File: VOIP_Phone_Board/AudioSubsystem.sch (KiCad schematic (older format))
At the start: 39 parts, among them J1 Headset, J5 Speaker, J6 Microphone, U1 PCM5102, U2 PCM1808PW, X1 SG-8002DC

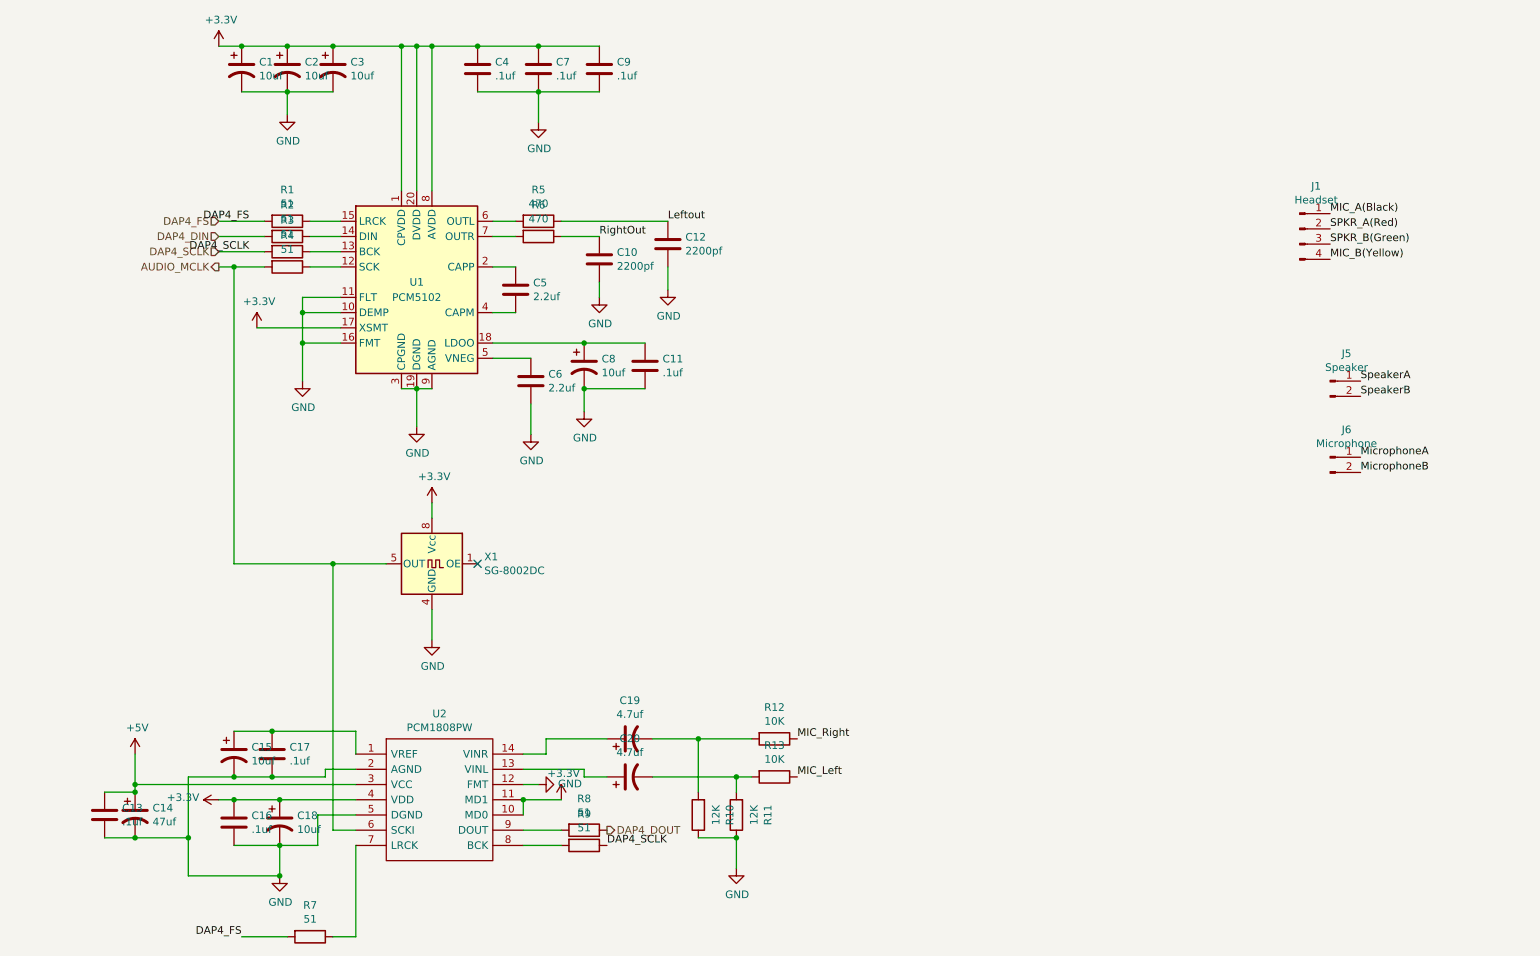
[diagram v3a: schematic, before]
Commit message: MAX98357A Version.
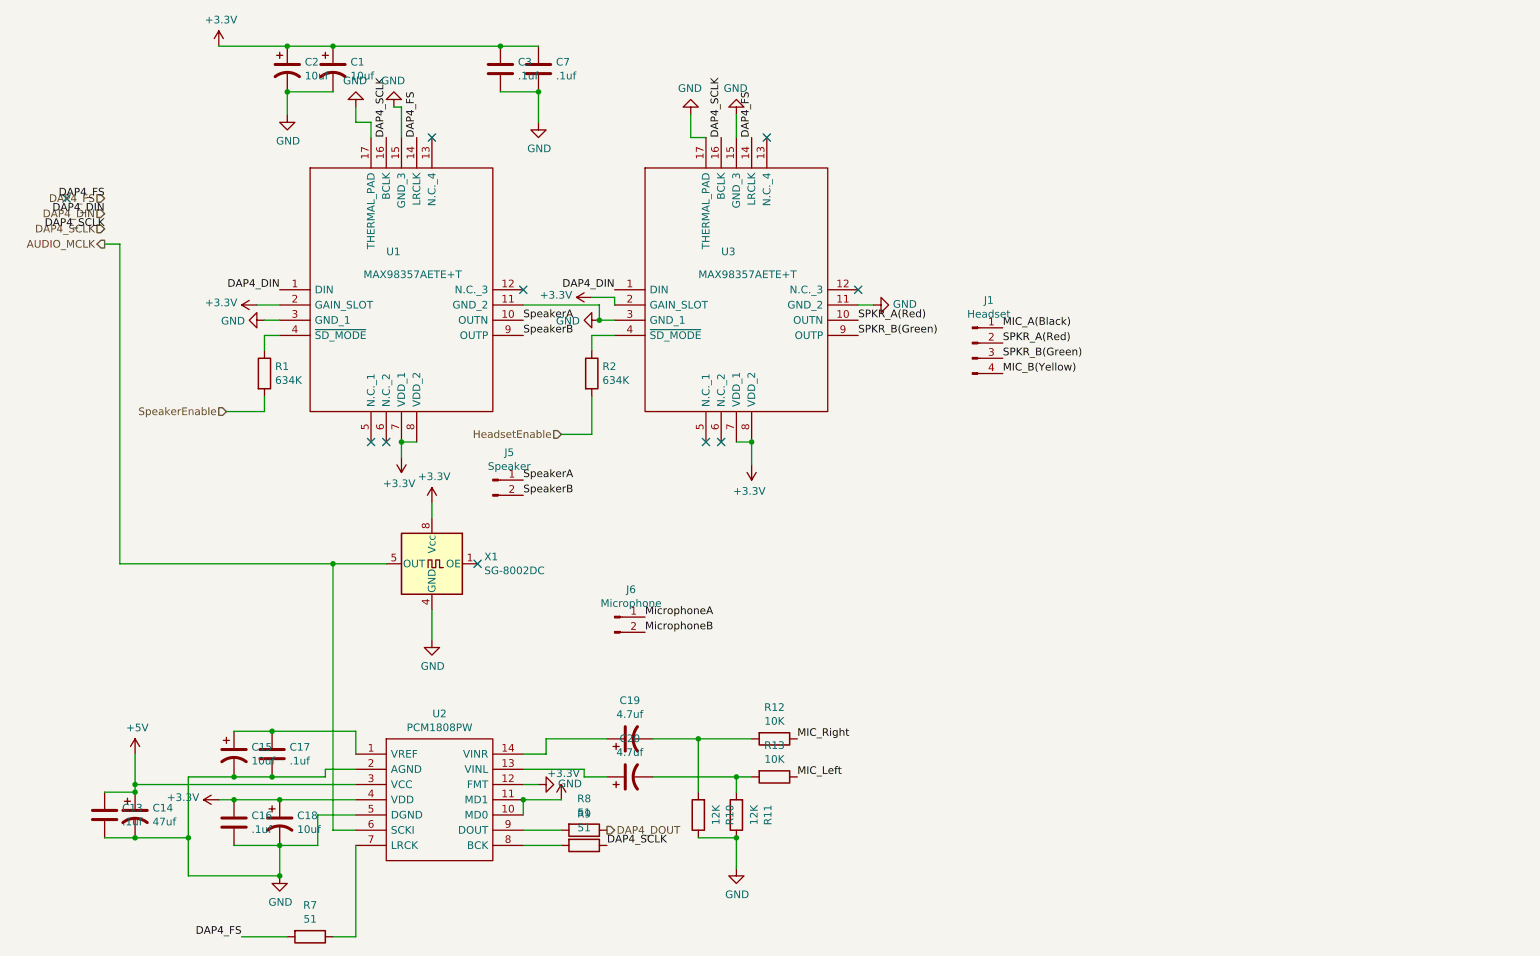
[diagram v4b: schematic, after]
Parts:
- removed C10, C12: 2200pf, Capacitor_THT:C_Rect_L4.0mm_W2.5mm_P2.50mm, symbol Device:C
- removed C11, C4, C9: .1uf, Capacitor_SMD:C_0603_1608Metric_Pad1.05x0.95mm_HandSolder, symbol Device:C
- removed C3, C8: 10uf, VOIP_Phone_Board:CP_0603_1608Metric_Pad1.05x0.95mm_HandSolder, symbol Device:CP1
- removed C5, C6: 2.2uf, Capacitor_SMD:C_0402_1005Metric, symbol Device:C
- removed R3, R4: 51, Resistor_SMD:R_0603_1608Metric_Pad1.05x0.95mm_HandSolder, symbol Device:R
- removed R5, R6: 470, Resistor_SMD:R_0603_1608Metric_Pad1.05x0.95mm_HandSolder, symbol Device:R
- removed U1: PCM5102, Package_SO:TSSOP-20_4.4x6.5mm_P0.65mm, symbol Audio:PCM5102
- added C3: .1uf, Capacitor_SMD:C_0603_1608Metric_Pad1.05x0.95mm_HandSolder, symbol Device:C
- added U1, U3: MAX98357AETE+T, QFN50P300X300X80-17N, symbol MAX98357AETE+T:MAX98357AETE+T
- R1, R2: value 51 -> 634K; Mouser Part Number 667-ERJ-PA3J510V -> 603-RT0603FRE07634KL
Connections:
- net +3V3: now also C3.1, U1.2 (GAIN_SLOT), U1.7 (VDD_1), U1.8 (VDD_2), U3.2 (GAIN_SLOT), U3.7 (VDD_1), U3.8 (VDD_2)
- net DAP4_DIN: now also U1.1 (DIN), U3.1 (DIN); no longer R2.2
- net DAP4_FS: now also U1.14 (LRCLK), U3.14 (LRCLK); no longer R1.2
- net DAP4_SCLK: now also U1.16 (BCLK), U3.16 (BCLK)
- net GND: now also C3.2, U1.11 (GND_2), U1.15 (GND_3), U1.17 (THERMAL_PAD), U1.3 (GND_1), U3.11 (GND_2), U3.15 (GND_3), U3.17 (THERMAL_PAD), U3.3 (GND_1)
- net SPKR_A(Red): now also U3.10 (OUTN)
- net SPKR_B(Green): now also U3.9 (OUTP)
- net SpeakerA: now also U1.10 (OUTN)
- net SpeakerB: now also U1.9 (OUTP)
- net at R2.1: now also U3.4 (~SD_MODE)
- net at R1.1: now also U1.4 (~SD_MODE)
- new net HeadsetEnable: R2.2
- new net SpeakerEnable: R1.2
- no-connect marks 1 -> 10
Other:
- moved on the sheet: J1, J5, J6

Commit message: Started with ADAU1361.
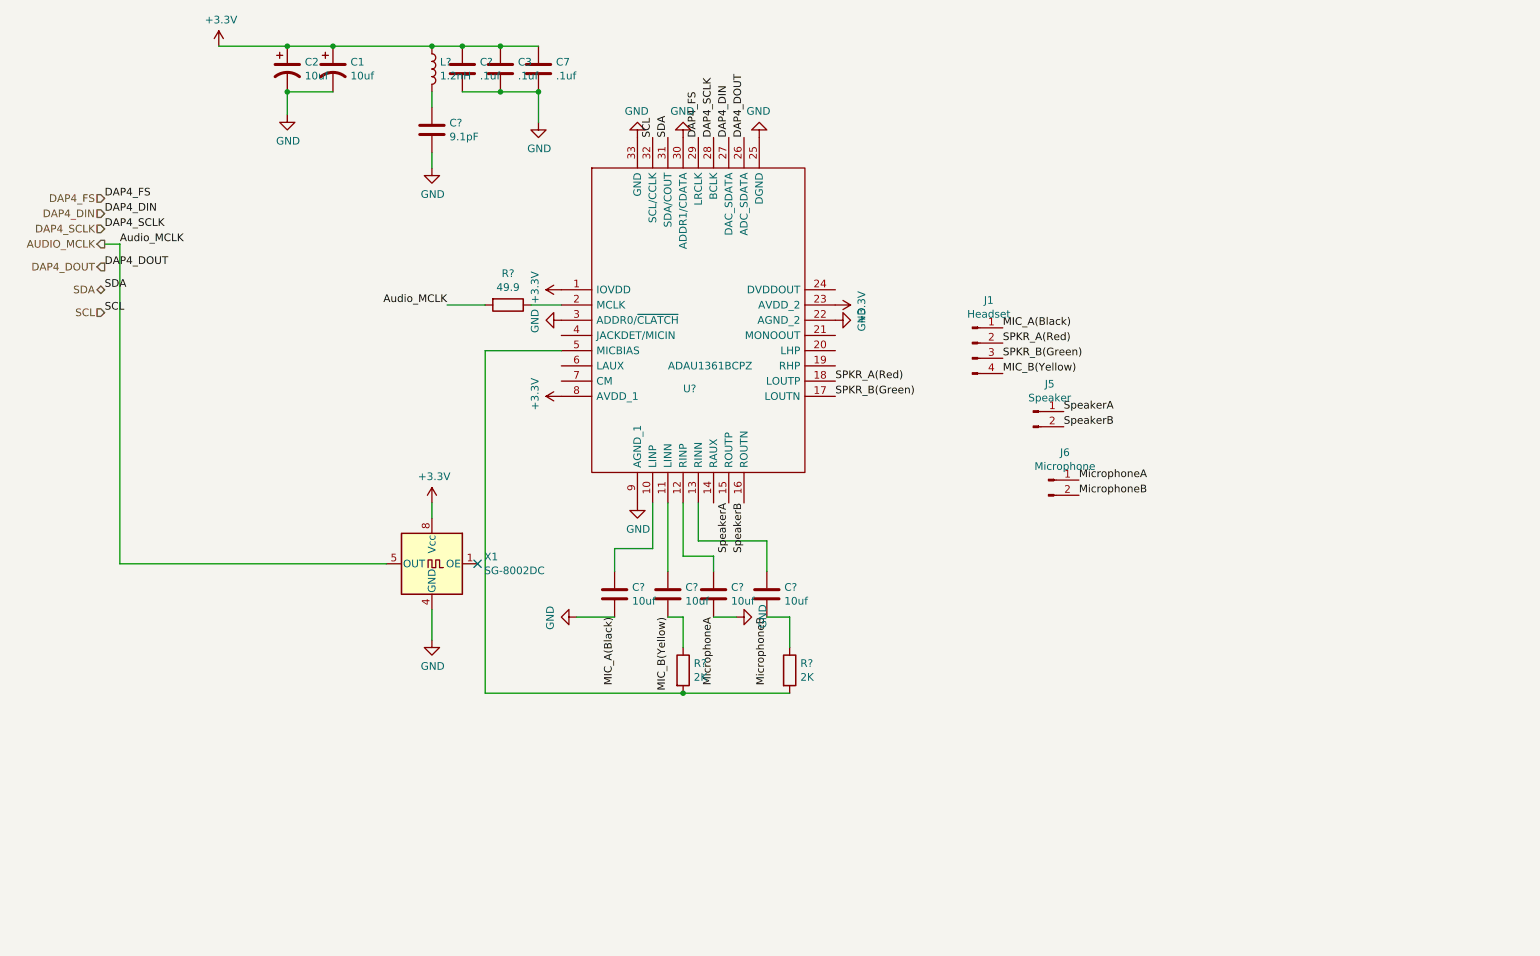
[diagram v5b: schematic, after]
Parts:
- removed C13, C16, C17: .1uf, Capacitor_SMD:C_0603_1608Metric_Pad1.05x0.95mm_HandSolder, symbol Device:C
- removed C14: 47uf, Capacitor_THT:CP_Radial_D6.3mm_P2.50mm, symbol Device:CP1
- removed C15, C18: 10uf, VOIP_Phone_Board:CP_0603_1608Metric_Pad1.05x0.95mm_HandSolder, symbol Device:CP1
- removed C19, C20: 4.7uf, VOIP_Phone_Board:CP_0603_1608Metric_Pad1.05x0.95mm_HandSolder, symbol Device:CP1
- removed R1, R2: 634K, Resistor_SMD:R_0603_1608Metric_Pad1.05x0.95mm_HandSolder, symbol Device:R
- removed R10, R11: 12K, Resistor_SMD:R_0603_1608Metric_Pad1.05x0.95mm_HandSolder, symbol Device:R
- removed R12, R13: 10K, Resistor_SMD:R_0603_1608Metric_Pad1.05x0.95mm_HandSolder, symbol Device:R
- removed R7, R8, R9: 51, Resistor_SMD:R_0603_1608Metric_Pad1.05x0.95mm_HandSolder, symbol Device:R
- removed U1, U3: MAX98357AETE+T, QFN50P300X300X80-17N, symbol MAX98357AETE+T:MAX98357AETE+T
- removed U2: PCM1808PW, VOIP_Phone_Board:SOP65P640X120-14N, symbol PCM1808PW:PCM1808PW
- added C?: .1uf, Capacitor_SMD:C_0603_1608Metric_Pad1.05x0.95mm_HandSolder, symbol Device:C
- added C?: 9.1pF, symbol Device:C
- added C? (x4): 10uf, symbol Device:C
- added L?: 1.2nH, symbol Device:L
- added R? (x2): 2K, symbol Device:R
- added R?: 49.9, symbol Device:R
- added U?: ADAU1361BCPZ, QFN50P500X500X100-33N-D, symbol ADAU1361BCPZ:ADAU1361BCPZ
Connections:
- net MIC_A(Black) is gone; now on net GND: J1.1 (Pin_1)
- net MicrophoneA is gone; now on net GND: J6.1 (Pin_1)
- net +3V3: now also C?.1, L?.1, U?.1 (IOVDD), U?.23 (AVDD_2), U?.8 (AVDD_1)
- net AUDIO_MCLK: now also R?.2
- net DAP4_DIN: now also U?.27 (DAC_SDATA)
- net DAP4_DOUT: now also U?.26 (ADC_SDATA)
- net DAP4_FS: now also U?.29 (LRCLK)
- net DAP4_SCLK: now also U?.28 (BCLK)
- net GND: now also C?.2, C?.2, C?.2, C?.2, U?.22 (AGND_2), U?.25 (DGND), U?.3 (ADDR0/~CLATCH), U?.30 (ADDR1/CDATA), U?.33 (GND), U?.9 (AGND_1)
- net MIC_B(Yellow): now also C?.2, R?.1
- net MicrophoneB: now also C?.2, R?.1
- net SPKR_A(Red): now also U?.18 (LOUTP)
- net SPKR_B(Green): now also U?.17 (LOUTN)
- net SpeakerA: now also U?.15 (ROUTP)
- net SpeakerB: now also U?.16 (ROUTN)
- new net: C?.1, U?.10 (LINP)
- new net: C?.1, U?.11 (LINN)
- new net: C?.1, U?.12 (RINP)
- new net: C?.1, U?.13 (RINN)
- new net: R?.1, U?.2 (MCLK)
- new net: R?.2, R?.2, U?.5 (MICBIAS)
- new net: C?.1, L?.2
- new net SCL: U?.32 (SCL/CCLK)
- new net SDA: U?.31 (SDA/COUT)
- no-connect marks 10 -> 1
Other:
- moved on the sheet: J5, J6
